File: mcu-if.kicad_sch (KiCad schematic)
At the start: 7 parts

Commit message: Add power supply.
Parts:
- added C?: 100n, Capacitor_SMD:C_0603_1608Metric_Pad1.08x0.95mm_HandSolder, symbol Device:C
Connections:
- net GND: now also C?.2
- net VDD: now also C?.1
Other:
- moved on the sheet: R?
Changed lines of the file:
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@@
   (junction (at 92.71 36.83) (diameter 0) (color 0 0 0 0)
   )
+  (junction (at 129.54 44.45) (diameter 0) (color 0 0 0 0)
+  )
   (junction (at 116.84 44.45) (diameter 0) (color 0 0 0 0)
   )
+  (junction (at 135.89 95.25) (diameter 0) (color 0 0 0 0)
+  )
   (junction (at 104.14 72.39) (diameter 0) (color 0 0 0 0)
   )
@@
     (stroke (width 0) (type default) (color 0 0 0 0))
   )
+  (wire (pts (xy 129.54 44.45) (xy 135.89 44.45))
+    (stroke (width 0) (type default) (color 0 0 0 0))
+  )
   (wire (pts (xy 104.14 44.45) (xy 104.14 58.42))
     (stroke (width 0) (type default) (color 0 0 0 0))
@@
     (stroke (width 0) (type default) (color 0 0 0 0))
   )
-  (wire (pts (xy 123.19 58.42) (xy 123.19 87.63))
+  (wire (pts (xy 123.19 66.04) (xy 123.19 87.63))
     (stroke (width 0) (type default) (color 0 0 0 0))
   )
@@
     (stroke (width 0) (type default) (color 0 0 0 0))
   )
-  (wire (pts (xy 151.13 82.55) (xy 154.94 82.55))
+  (wire (pts (xy 135.89 66.04) (xy 135.89 95.25))
     (stroke (width 0) (type default) (color 0 0 0 0))
   )
@@
     (stroke (width 0) (type default) (color 0 0 0 0))
   )
-  (wire (pts (xy 129.54 58.42) (xy 129.54 44.45))
+  (wire (pts (xy 129.54 50.8) (xy 129.54 44.45))
     (stroke (width 0) (type default) (color 0 0 0 0))
   )
@@
     (stroke (width 0) (type default) (color 0 0 0 0))
   )
-  (wire (pts (xy 129.54 66.04) (xy 129.54 90.17))
+  (wire (pts (xy 129.54 58.42) (xy 129.54 90.17))
+    (stroke (width 0) (type default) (color 0 0 0 0))
+  )
+  (wire (pts (xy 135.89 95.25) (xy 203.2 95.25))
     (stroke (width 0) (type default) (color 0 0 0 0))
   )
@@
     (stroke (width 0) (type default) (color 0 0 0 0))
   )
+  (wire (pts (xy 135.89 44.45) (xy 135.89 58.42))
+    (stroke (width 0) (type default) (color 0 0 0 0))
+  )
   (wire (pts (xy 97.79 85.09) (xy 154.94 85.09))
     (stroke (width 0) (type default) (color 0 0 0 0))
@@
     (stroke (width 0) (type default) (color 0 0 0 0))
   )
-  (wire (pts (xy 97.79 95.25) (xy 203.2 95.25))
-    (stroke (width 0) (type default) (color 0 0 0 0))
-  )
-  (wire (pts (xy 95.25 82.55) (xy 143.51 82.55))
+  (wire (pts (xy 97.79 95.25) (xy 135.89 95.25))
+    (stroke (width 0) (type default) (color 0 0 0 0))
+  )
+  (wire (pts (xy 95.25 82.55) (xy 147.32 82.55))
     (stroke (width 0) (type default) (color 0 0 0 0))
   )
@@
     (stroke (width 0) (type default) (color 0 0 0 0))
   )
-  (wire (pts (xy 123.19 50.8) (xy 123.19 44.45))
+  (wire (pts (xy 123.19 58.42) (xy 123.19 44.45))
     (stroke (width 0) (type default) (color 0 0 0 0))
   )
@@
     (effects (font (size 1.27 1.27)) (justify right bottom))
   )
-  (label "SDMMC.CK" (at 143.51 82.55 180)
+  (label "SDMMC.CK" (at 147.32 82.55 180)
     (effects (font (size 1.27 1.27)) (justify right bottom))
   )
@@
   (hierarchical_label "SDMMC" (shape bidirectional) (at 88.9 36.83 180)
     (effects (font (size 1.27 1.27)) (justify right))
+  )
+  (symbol (lib_id "Device:C") (at 135.89 62.23 0) (unit 1)
+    (in_bom yes) (on_board yes) (fields_autoplaced)
+    (property "Reference" "C?" (id 0) (at 138.811 61.3953 0)
+      (effects (font (size 1.27 1.27)) (justify left))
+    )
+    (property "Value" "100n" (id 1) (at 138.811 63.9322 0)
+      (effects (font (size 1.27 1.27)) (justify left))
+    )
+    (property "Footprint" "Capacitor_SMD:C_0603_1608Metric_Pad1.08x0.95mm_HandSolder" (id 2) (at 136.8552 66.04 0)
+      (effects (font (size 1.27 1.27)) hide)
+    )
+    (property "Datasheet" "~" (id 3) (at 135.89 62.23 0)
+      (effects (font (size 1.27 1.27)) hide)
+    )
+    (pin "1")
+    (pin "2")
   )
   (symbol (lib_id "Connector:SD_Card") (at 177.8 80.01 0) (unit 1)
@@
     (pin "1")
   )
-  (symbol (lib_id "Device:R") (at 147.32 82.55 90) (unit 1)
+  (symbol (lib_id "Device:R") (at 151.13 82.55 90) (unit 1)
     (in_bom yes) (on_board yes)
-    (property "Reference" "R?" (id 0) (at 147.32 82.55 90))
-    (property "Value" "100" (id 1) (at 147.32 80.3711 90))
-    (property "Footprint" "" (id 2) (at 147.32 84.328 90)
-      (effects (font (size 1.27 1.27)) hide)
-    )
-    (property "Datasheet" "~" (id 3) (at 147.32 82.55 0)
-      (effects (font (size 1.27 1.27)) hide)
-    )
-    (pin "1")
-    (pin "2")
-  )
-  (symbol (lib_id "Device:R") (at 123.19 54.61 0) (unit 1)
-    (in_bom yes) (on_board yes) (fields_autoplaced)
-    (property "Reference" "R?" (id 0) (at 124.968 53.7753 0)
-      (effects (font (size 1.27 1.27)) (justify left))
-    )
-    (property "Value" "47k" (id 1) (at 124.968 56.3122 0)
-      (effects (font (size 1.27 1.27)) (justify left))
-    )
-    (property "Footprint" "" (id 2) (at 121.412 54.61 90)
-      (effects (font (size 1.27 1.27)) hide)
-    )
-    (property "Datasheet" "~" (id 3) (at 123.19 54.61 0)
+    (property "Reference" "R?" (id 0) (at 151.13 82.55 90))
+    (property "Value" "100" (id 1) (at 151.13 80.3711 90))
+    (property "Footprint" "" (id 2) (at 151.13 84.328 90)
+      (effects (font (size 1.27 1.27)) hide)
+    )
+    (property "Datasheet" "~" (id 3) (at 151.13 82.55 0)
+      (effects (font (size 1.27 1.27)) hide)
+    )
+    (pin "1")
+    (pin "2")
+  )
+  (symbol (lib_id "Device:R") (at 123.19 62.23 0) (unit 1)
+    (in_bom yes) (on_board yes) (fields_autoplaced)
+    (property "Reference" "R?" (id 0) (at 124.968 61.3953 0)
+      (effects (font (size 1.27 1.27)) (justify left))
+    )
+    (property "Value" "47k" (id 1) (at 124.968 63.9322 0)
+      (effects (font (size 1.27 1.27)) (justify left))
+    )
+    (property "Footprint" "" (id 2) (at 121.412 62.23 90)
+      (effects (font (size 1.27 1.27)) hide)
+    )
+    (property "Datasheet" "~" (id 3) (at 123.19 62.23 0)
       (effects (font (size 1.27 1.27)) hide)
     )
@@
     (pin "1")
   )
-  (symbol (lib_id "Device:R") (at 129.54 62.23 0) (unit 1)
-    (in_bom yes) (on_board yes) (fields_autoplaced)
-    (property "Reference" "R?" (id 0) (at 131.318 61.3953 0)
-      (effects (font (size 1.27 1.27)) (justify left))
-    )
-    (property "Value" "47k" (id 1) (at 131.318 63.9322 0)
-      (effects (font (size 1.27 1.27)) (justify left))
-    )
-    (property "Footprint" "" (id 2) (at 127.762 62.23 90)
-      (effects (font (size 1.27 1.27)) hide)
-    )
-    (property "Datasheet" "~" (id 3) (at 129.54 62.23 0)
-      (effects (font (size 1.27 1.27)) hide)
-    )
+  (symbol (lib_id "Device:R") (at 129.54 54.61 0) (unit 1)
+    (in_bom yes) (on_board yes) (fields_autoplaced)
+    (property "Reference" "R?" (id 0) (at 131.318 53.7753 0)
+      (effects (font (size 1.27 1.27)) (justify left))
+    )
+    (property "Value" "47k" (id 1) (at 131.318 56.3122 0)
+      (effects (font (size 1.27 1.27)) (justify left))
+    )
+    (property "Footprint" "" (id 2) (at 127.762 54.61 90)
+      (effects (font (size 1.27 1.27)) hide)
+    )
+    (property "Datasheet" "~" (id 3) (at 129.54 54.61 0)
+      (effects (font (size 1.27 1.27)) hide)
+    )

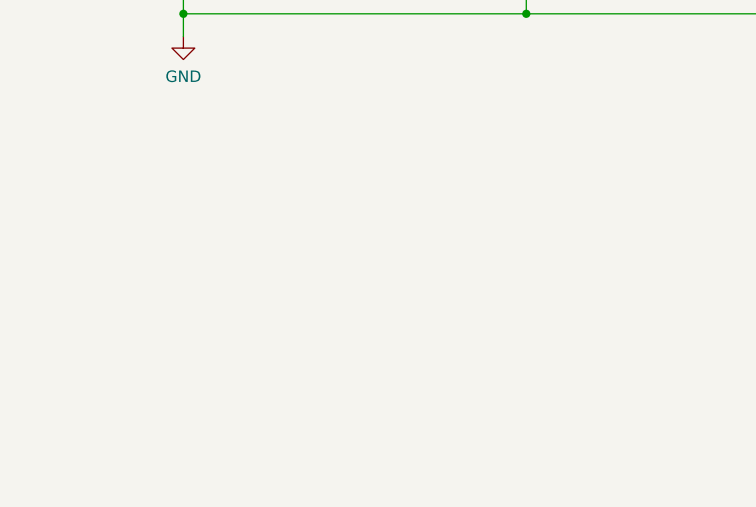
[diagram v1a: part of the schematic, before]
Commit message: Add MCU USB
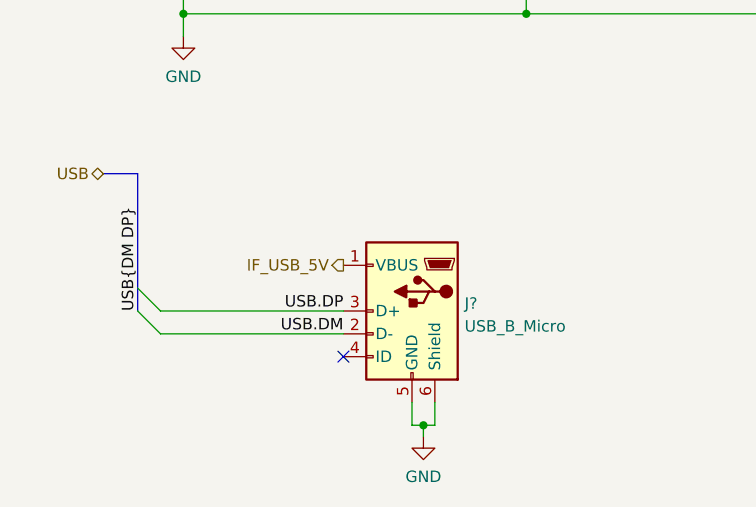
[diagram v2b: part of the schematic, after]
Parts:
- added J?: USB_B_Micro, symbol Connector:USB_B_Micro
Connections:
- net GND: now also J?.5 (GND), J?.6 (Shield)
- new net IF_USB_5V: J?.1 (VBUS)
- new net USB.DM: J?.2 (D-)
- new net USB.DP: J?.3 (D+)
- no-connect marks 0 -> 1
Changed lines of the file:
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@@
   (junction (at 110.49 44.45) (diameter 0) (color 0 0 0 0)
   )
+  (junction (at 124.46 140.97) (diameter 0) (color 0 0 0 0)
+  )
   (junction (at 97.79 95.25) (diameter 0) (color 0 0 0 0)
   )
@@
   (junction (at 97.79 85.09) (diameter 0) (color 0 0 0 0)
   )
+  (no_connect (at 115.57 133.35))
   (bus_entry (at 92.71 67.31) (size 2.54 2.54)
     (stroke (width 0) (type default) (color 0 0 0 0))
@@
     (stroke (width 0) (type default) (color 0 0 0 0))
   )
+  (bus_entry (at 92.71 125.73) (size 2.54 2.54)
+    (stroke (width 0) (type default) (color 0 0 0 0))
+  )
   (bus_entry (at 92.71 85.09) (size 2.54 2.54)
     (stroke (width 0) (type default) (color 0 0 0 0))
@@
     (stroke (width 0) (type default) (color 0 0 0 0))
   )
+  (bus_entry (at 92.71 128.27) (size 2.54 2.54)
+    (stroke (width 0) (type default) (color 0 0 0 0))
+  )
   (bus_entry (at 92.71 72.39) (size 2.54 2.54)
     (stroke (width 0) (type default) (color 0 0 0 0))
@@
     (stroke (width 0) (type default) (color 0 0 0 0))
   )
+  (wire (pts (xy 95.25 128.27) (xy 115.57 128.27))
+    (stroke (width 0) (type default) (color 0 0 0 0))
+  )
+  (bus (pts (xy 92.71 125.73) (xy 92.71 128.27))
+    (stroke (width 0) (type default) (color 0 0 0 0))
+  )
   (wire (pts (xy 104.14 44.45) (xy 110.49 44.45))
     (stroke (width 0) (type default) (color 0 0 0 0))
@@
     (stroke (width 0) (type default) (color 0 0 0 0))
   )
+  (wire (pts (xy 125.73 140.97) (xy 125.73 138.43))
+    (stroke (width 0) (type default) (color 0 0 0 0))
+  )
   (wire (pts (xy 154.94 77.47) (xy 97.79 77.47))
     (stroke (width 0) (type default) (color 0 0 0 0))
@@
     (stroke (width 0) (type default) (color 0 0 0 0))
   )
+  (wire (pts (xy 124.46 142.24) (xy 124.46 140.97))
+    (stroke (width 0) (type default) (color 0 0 0 0))
+  )
   (wire (pts (xy 97.79 85.09) (xy 154.94 85.09))
     (stroke (width 0) (type default) (color 0 0 0 0))
@@
     (stroke (width 0) (type default) (color 0 0 0 0))
   )
+  (wire (pts (xy 123.19 140.97) (xy 124.46 140.97))
+    (stroke (width 0) (type default) (color 0 0 0 0))
+  )
   (wire (pts (xy 97.79 44.45) (xy 97.79 50.8))
     (stroke (width 0) (type default) (color 0 0 0 0))
   )
+  (wire (pts (xy 123.19 140.97) (xy 123.19 138.43))
+    (stroke (width 0) (type default) (color 0 0 0 0))
+  )
+  (bus (pts (xy 88.9 113.03) (xy 92.71 113.03))
+    (stroke (width 0) (type default) (color 0 0 0 0))
+  )
   (wire (pts (xy 97.79 44.45) (xy 104.14 44.45))
     (stroke (width 0) (type default) (color 0 0 0 0))
@@
     (stroke (width 0) (type default) (color 0 0 0 0))
   )
+  (bus (pts (xy 92.71 113.03) (xy 92.71 125.73))
+    (stroke (width 0) (type default) (color 0 0 0 0))
+  )
   (wire (pts (xy 95.25 82.55) (xy 147.32 82.55))
     (stroke (width 0) (type default) (color 0 0 0 0))
@@
     (stroke (width 0) (type default) (color 0 0 0 0))
   )
+  (wire (pts (xy 124.46 140.97) (xy 125.73 140.97))
+    (stroke (width 0) (type default) (color 0 0 0 0))
+  )
+  (wire (pts (xy 95.25 130.81) (xy 115.57 130.81))
+    (stroke (width 0) (type default) (color 0 0 0 0))
+  )
   (bus (pts (xy 215.9 36.83) (xy 215.9 72.39))
     (stroke (width 0) (type default) (color 0 0 0 0))
@@
   (bus (pts (xy 92.71 36.83) (xy 92.71 67.31))
     (stroke (width 0) (type default) (color 0 0 0 0))
+  )
+  (label "USB.DM" (at 115.57 130.81 180)
+    (effects (font (size 1.27 1.27)) (justify right bottom))
+  )
+  (label "USB{DM DP}" (at 92.71 128.27 90)
+    (effects (font (size 1.27 1.27)) (justify left bottom))
   )
   (label "SDMMC.D3" (at 154.94 72.39 180)
@@
     (effects (font (size 1.27 1.27)) (justify right bottom))
   )
+  (label "USB.DP" (at 115.57 128.27 180)
+    (effects (font (size 1.27 1.27)) (justify right bottom))
+  )
   (label "SDMMC.D1" (at 154.94 90.17 180)
     (effects (font (size 1.27 1.27)) (justify right bottom))
@@
   (label "SDMMC.CD" (at 200.66 74.93 0)
     (effects (font (size 1.27 1.27)) (justify left bottom))
+  )
+  (hierarchical_label "IF_USB_5V" (shape output) (at 115.57 123.19 180)
+    (effects (font (size 1.27 1.27)) (justify right))
+  )
+  (hierarchical_label "USB" (shape bidirectional) (at 88.9 113.03 180)
+    (effects (font (size 1.27 1.27)) (justify right))
   )
   (hierarchical_label "SDMMC" (shape bidirectional) (at 88.9 36.83 180)
@@
     (pin "2")
   )
+  (symbol (lib_id "power:GND") (at 124.46 142.24 0) (unit 1)
+    (in_bom yes) (on_board yes) (fields_autoplaced)
+    (property "Reference" "#PWR?" (id 0) (at 124.46 148.59 0)
+      (effects (font (size 1.27 1.27)) hide)
+    )
+    (property "Value" "GND" (id 1) (at 124.46 146.6834 0))
+    (property "Footprint" "" (id 2) (at 124.46 142.24 0)
+      (effects (font (size 1.27 1.27)) hide)
+    )
+    (property "Datasheet" "" (id 3) (at 124.46 142.24 0)
+      (effects (font (size 1.27 1.27)) hide)
+    )
+    (pin "1")
+  )
   (symbol (lib_id "Device:R") (at 123.19 62.23 0) (unit 1)
     (in_bom yes) (on_board yes) (fields_autoplaced)
@@
     (pin "2")
   )
+  (symbol (lib_id "Connector:USB_B_Micro") (at 123.19 128.27 0) (mirror y) (unit 1)
+    (in_bom yes) (on_board yes) (fields_autoplaced)
+    (property "Reference" "J?" (id 0) (at 129.032 127.4353 0)
+      (effects (font (size 1.27 1.27)) (justify right))
+    )
+    (property "Value" "USB_B_Micro" (id 1) (at 129.032 129.9722 0)
+      (effects (font (size 1.27 1.27)) (justify right))
+    )
+    (property "Footprint" "" (id 2) (at 119.38 129.54 0)
+      (effects (font (size 1.27 1.27)) hide)
+    )
+    (property "Datasheet" "~" (id 3) (at 119.38 129.54 0)
+      (effects (font (size 1.27 1.27)) hide)
+    )
+    (pin "1")
+    (pin "2")
+    (pin "3")
+    (pin "4")
+    (pin "5")
+    (pin "6")
+  )
   (symbol (lib_id "Device:R") (at 110.49 54.61 0) (unit 1)
